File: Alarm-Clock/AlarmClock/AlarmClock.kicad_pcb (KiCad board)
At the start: 2 copper layers, 69.8 x 50 mm, 38 parts, among them J1 Jack-DC, J2 output, J3 ISP, SW1 SW_Set, SW2 SW_Inc, SW3 SW_Dec, U1 ATmega8A-A, U2 LM7805_TO220, U5 CC56-12GWA, Y1 Crystal

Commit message: Fixing bugs
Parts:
- added C6: 18pF, Capacitor_SMD:C_0603_1608Metric, F.Cu at (112.2, 108.0)
- added C7: 18pF, Capacitor_SMD:C_0603_1608Metric, F.Cu at (112.2, 109.5)
- D2: footprint Diode_THT:D_DO-35_SOD27_P7.62mm_Horizontal -> Diode_SMD:D_SMA; moved to B.Cu
- J3: footprint Connector_PinHeader_2.54mm:PinHeader_2x03_P2.54mm_Vertical -> Connector_IDC:IDC-Header_2x03_P2.54mm_Vertical; moved to B.Cu
- U2: value LM7805_TO220 -> L7805; footprint Package_TO_SOT_THT:TO-220-3_Vertical -> Package_TO_SOT_THT:TO-220-3_Horizontal_TabDown
- Y1: value Crystal -> 32K768
- moved D3 7.78 mm to (108.7, 114.3), turned to 0 degrees
- moved J3 5.58 mm to (133.8, 109.9)
- moved C2 5.09 mm to (109.0, 101.8), turned to 180 degrees
- moved U2 4.82 mm to (108.7, 108.8)
- moved J1 4.28 mm to (94.2, 113.5)
- moved R7 2.54 mm to (108.7, 112.4), turned to 0 degrees
- moved D2 2.46 mm to (99.0, 108.0)
- moved C1 1.73 mm to (108.7, 110.9), turned to 180 degrees
- moved Y1 0.93 mm to (114.8, 109.2), turned to 0 degrees
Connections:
- C3 pad 1: Net-(U1-PB1) -> Net-(U1-ADC7)
- C4 pad 1: Net-(U1-PB2) -> Net-(U1-PB1)
- C5 pad 1: /MOSI -> Net-(U1-PB2)
- R1 pad 2: Net-(U1-PB1) -> Net-(U1-ADC7)
- R4 pad 2: Net-(U1-PB2) -> Net-(U1-PB1)
- R6 pad 2: /MOSI -> Net-(U1-PB2)
- U1 pad 22: unconnected-(U1-ADC7-Pad22) -> Net-(U1-ADC7)
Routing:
- net +5C: track 138.9 -> 78.2 mm, vias 2 -> 3
- net Net-(U1-ADC7): track 0.00 -> 18.6 mm, vias 0 -> 2
- net Net-(U1-PB2): track 4.39 -> 11.0 mm
- net /MOSI: track 23.7 -> 17.3 mm, vias 1 -> 0
- net GND: track 145.4 -> 139.4 mm, vias 7 -> 3
- net Net-(U1-PD5): track 38.6 -> 33.3 mm
- net Net-(U1-PB1): track 9.91 -> 4.70 mm
- net /MISO: track 12.0 -> 6.97 mm, vias 1 -> 0
- net Net-(U1-PB6/XTAL1): track 4.93 -> 7.89 mm, vias 1 -> 0
- net Net-(U1-PB7/XTAL2): track 5.03 -> 7.97 mm, vias 1 -> 0
- net Net-(J3-Pin_5): track 14.7 -> 12.0 mm
- net +12C: track 14.8 -> 12.2 mm, vias 1 -> 0
- net Net-(U1-PD7): track 16.5 -> 19.0 mm
- net Net-(D2-A): track 5.83 -> 7.47 mm
- net /SCK: track 7.35 -> 5.98 mm, vias 1 -> 0
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
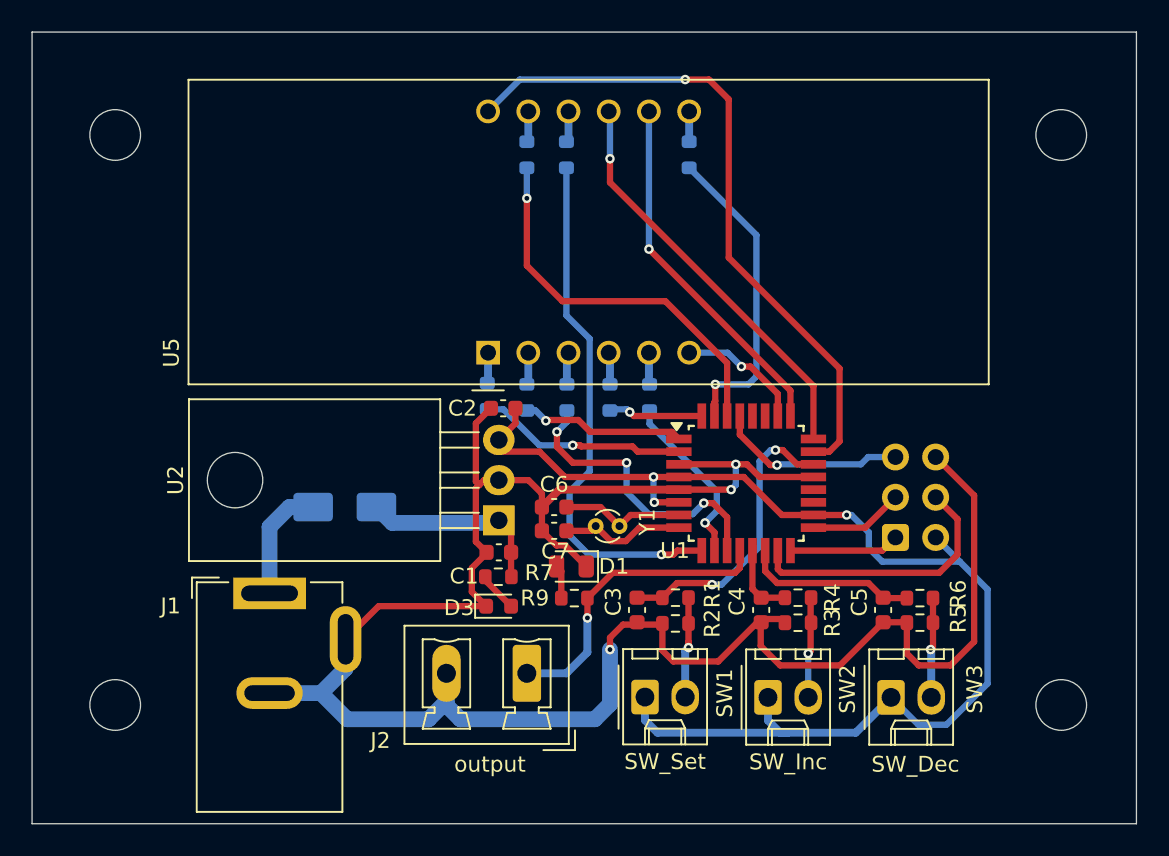
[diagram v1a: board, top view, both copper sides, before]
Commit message: Updating/Improving PCB. Adding ground plane, making crystal SMD, some alignments and cleanups. Adding missing crystal capacitors.
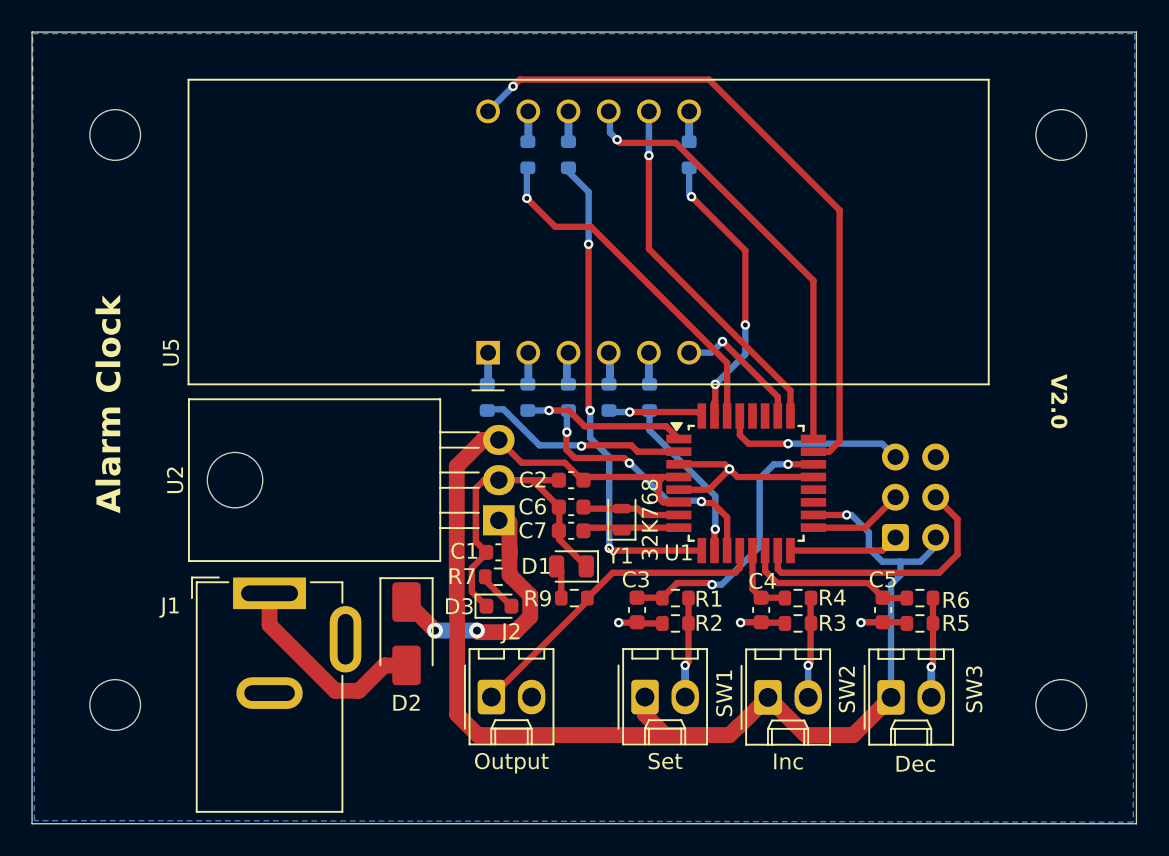
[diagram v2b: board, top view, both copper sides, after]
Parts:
- D2: moved to F.Cu
- J2: value output -> Output; footprint Connector_Phoenix_MC_HighVoltage:PhoenixContact_MCV_1,5_2-G-5.08_1x02_P5.08mm_Vertical -> Connector_Molex:Molex_KK-254_AE-6410-02A_1x02_P2.54mm_Vertical
- SW1: value SW_Set -> Set
- SW2: value SW_Inc -> Inc
- SW3: value SW_Dec -> Dec
- Y1: footprint Crystal:Crystal_Round_D1.0mm_Vertical -> Crystal:Crystal_SMD_2012-2Pin_2.0x1.2mm
- moved D2 8.90 mm to (102.9, 116.0), turned to -90 degrees
- moved C2 6.25 mm to (113.3, 106.3)
- moved J2 2.70 mm to (108.3, 120.0), turned to 0 degrees
- moved Y1 1.70 mm to (116.5, 108.8), turned to 90 degrees
- moved C6 1.08 mm to (113.3, 108.0)
- moved C7 1.08 mm to (113.3, 109.5)
- moved R15 0.12 mm to (113.1, 85.8)
- moved R17 0.09 mm to (113.1, 101.1)
- moved R14 0.08 mm to (108.0, 101.1)
- moved R10 0.06 mm to (110.6, 85.8)
- moved R12 0.06 mm to (115.7, 101.1)
- moved R13 0.06 mm to (110.6, 101.1)
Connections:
- J1 pad 3: GND -> (no net)
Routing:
- net GND: track 139.4 -> 41.6 mm, vias 3 -> 4
- net +5C: track 78.2 -> 87.1 mm, vias 3 -> 1
- net Net-(D2-A): track 7.47 -> 13.0 mm
- net +12C: track 12.2 -> 16.1 mm, vias 0 -> 2
- net Net-(U1-PD0): track 24.7 -> 22.2 mm
- net Net-(U1-PD7): track 19.0 -> 16.6 mm
- net Net-(U1-PD5): track 33.3 -> 31.0 mm, vias 1 -> 3
- net Net-(U1-PC1): track 26.0 -> 28.0 mm
- net Net-(U1-PB7/XTAL2): track 7.97 -> 6.08 mm
- net Net-(U1-PD1): track 19.8 -> 18.0 mm, vias 1 -> 3
- net Net-(U1-PB6/XTAL1): track 7.89 -> 6.21 mm
- net Net-(U1-ADC7): track 18.6 -> 17.2 mm
- net Net-(J2-Pin_1): track 19.3 -> 20.1 mm, vias 1 -> 0
- net Net-(U1-PD6): track 11.2 -> 10.6 mm
- added copper zone on B.Cu, net GND
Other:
- board text added: "Alarm Clock"
- board text added: "V2.0"
